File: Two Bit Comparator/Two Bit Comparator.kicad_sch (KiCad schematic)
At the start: 0 parts

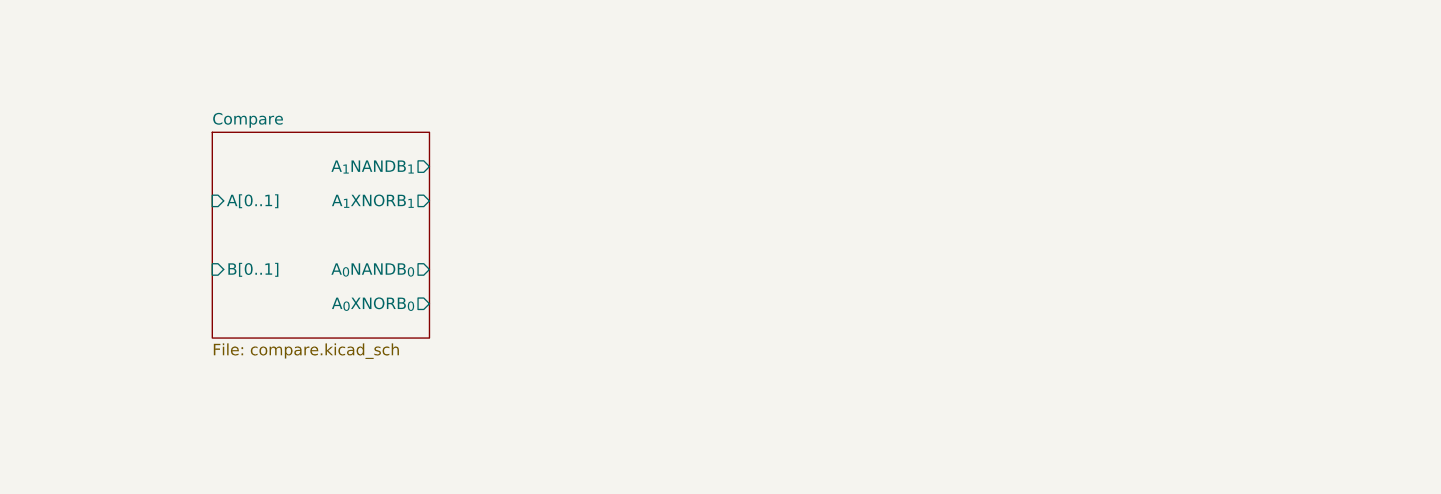
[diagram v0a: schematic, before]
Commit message: Starting on accumulation/output stage
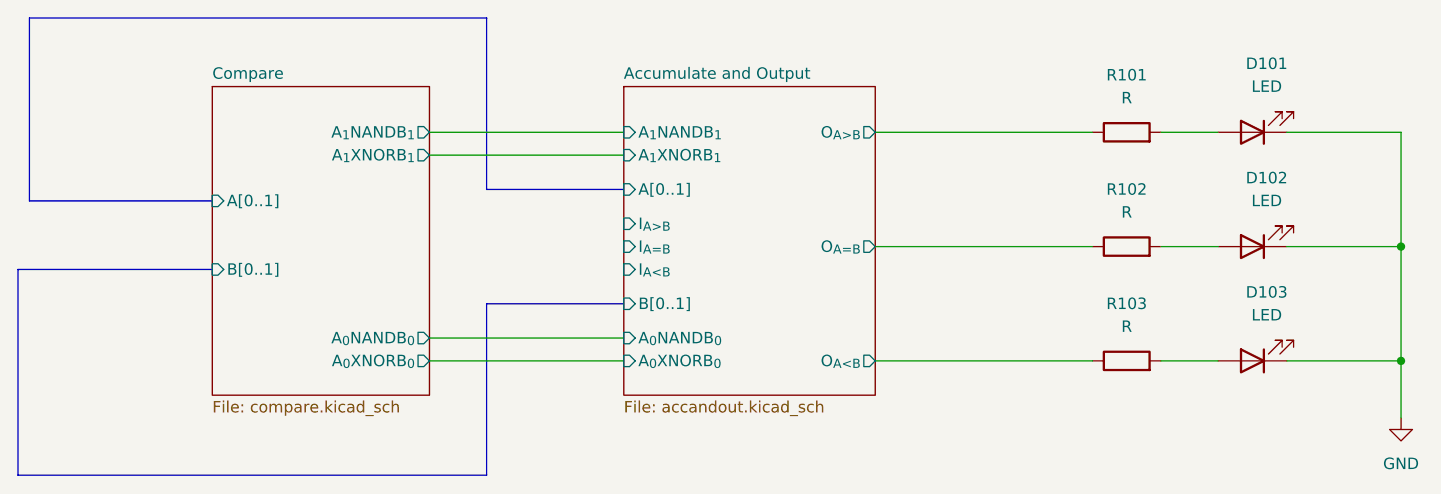
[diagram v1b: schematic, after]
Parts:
- added D101, D102, D103: LED, LED_THT:LED_D5.0mm, symbol Device:LED
- added R101, R102, R103: R, Resistor_THT:R_Axial_DIN0207_L6.3mm_D2.5mm_P7.62mm_Horizontal, symbol Device:R
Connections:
- new net: D101.2 (A), R101.2
- new net: D102.2 (A), R102.2
- new net: D103.2 (A), R103.2
- new net Accumulate and Output/O_{A<B}: R103.1
- new net Accumulate and Output/O_{A=B}: R102.1
- new net Accumulate and Output/O_{A>B}: R101.1
- new net GND: D101.1 (K), D102.1 (K), D103.1 (K)
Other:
- added sheet Accumulate and Output (accandout.kicad_sch)
